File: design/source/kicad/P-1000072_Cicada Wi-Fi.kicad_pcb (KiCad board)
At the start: 2 copper layers, 40 x 65 mm, 67 parts, among them J3 Host, U1 HX3406, U3 ESP-07S

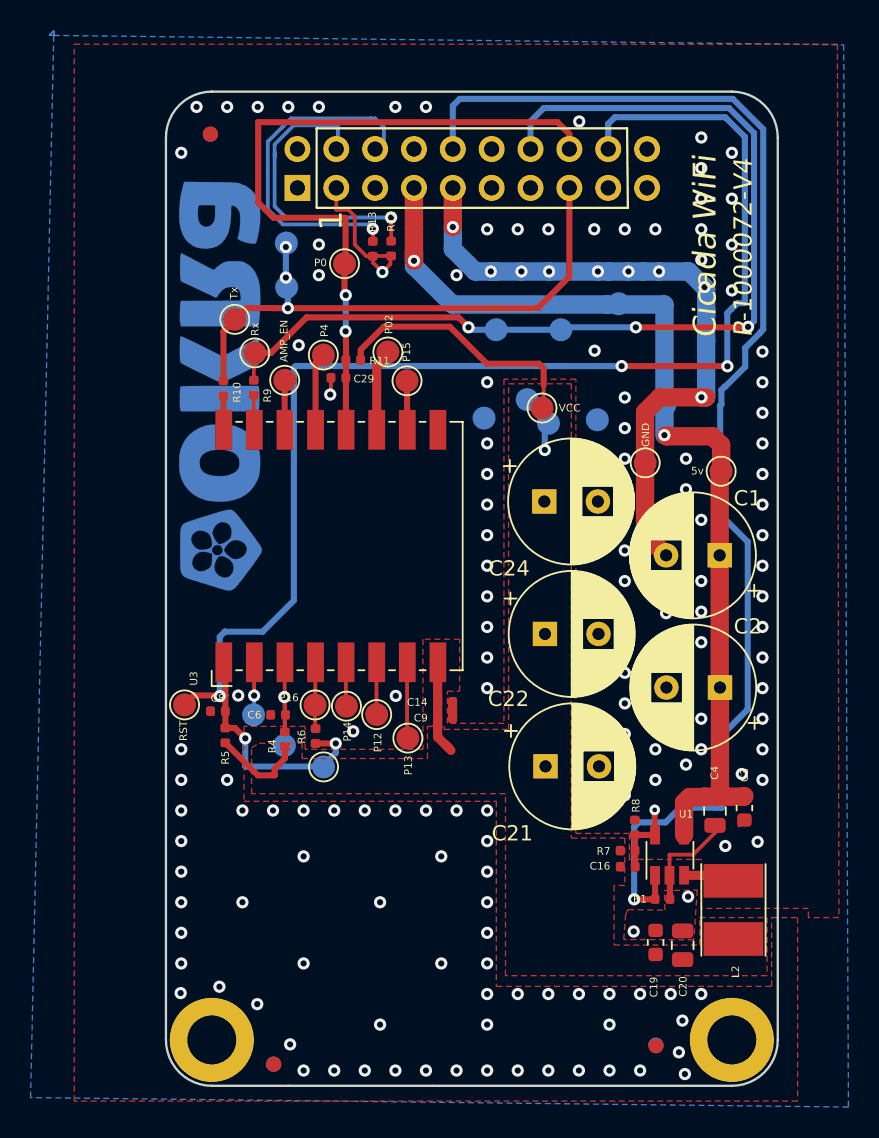
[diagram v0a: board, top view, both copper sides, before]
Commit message: P-1000072-V5.1.0_Cicada Wi-Fi Design and Manufacturing files update
Design update
1.)Inductor L2 Foot-print dimensions changed to parts commanded Foot-print dimensions(check for more information:design\doc\review\2022-03 Seed studios)
Manufacturing update
1.)updated manufacturing output files for the design change (L2 foot-print dimensions)
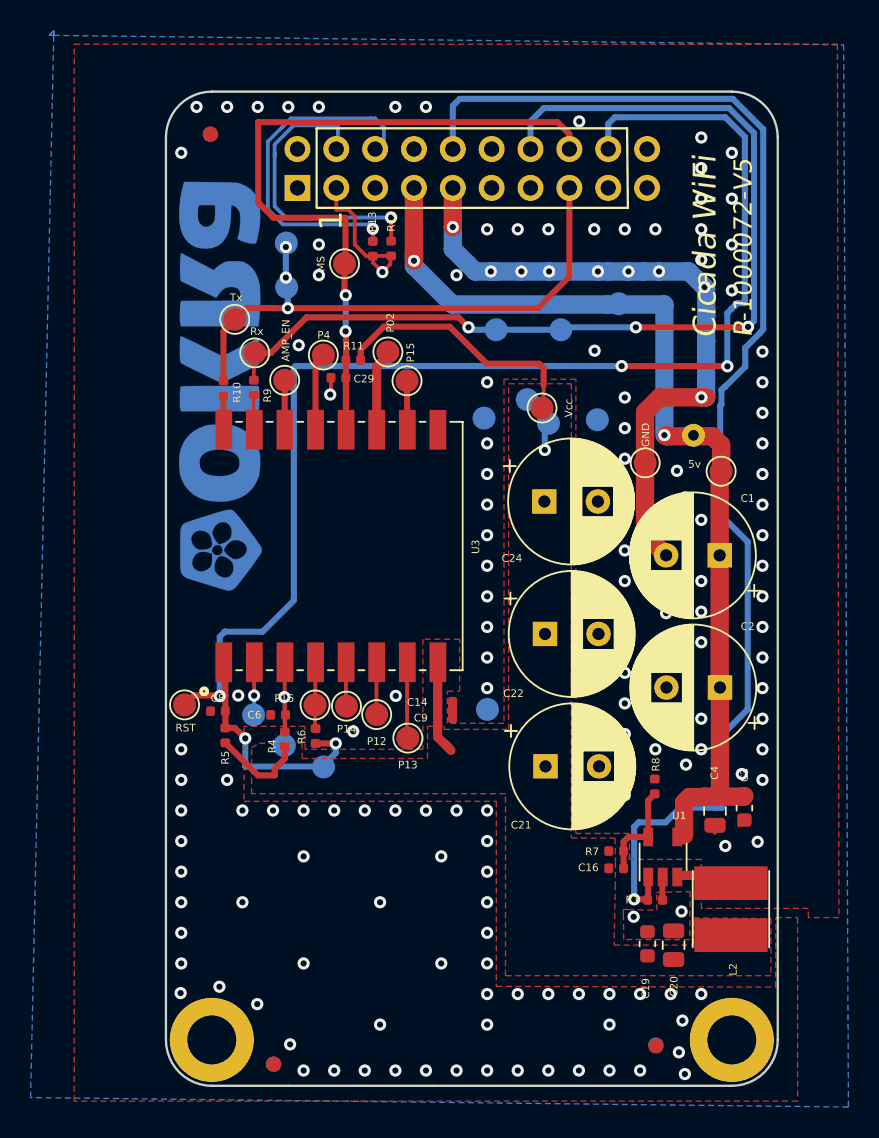
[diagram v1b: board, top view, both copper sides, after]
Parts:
- removed TP2: 5v, edemame-custom-footprints:TestPoint_Pad_D1.5mm
- added 5V: 5v, TestPoint:TestPoint_THTPad_D1.5mm_Drill0.7mm, B.Cu at (145.5, 82.5)
- added TP39: GND, okra-footprints:TestPoint_Pad_D1.5mm, B.Cu at (132.0, 100.4)
- J3: footprint cicada-footprints:PinSocket_2x08_P2.54mm_Vertical_padded -> Cicada-footprints:PinSocket_2x08_P2.54mm_Vertical_padded
- L2: footprint edemame-custom-footprints:L_4030_Handsoldering -> Cicada-footprints:L_4030_Handsoldering
- LOGO1: footprint cicada-footprints:okra_logo_copper_2 -> Cicada-footprints:okra_logo_copper_2
- TP1, TP12, TP13, TP14, TP15, TP16, TP23, TP24, TP25, TP26, TP27, TP28, TP29, TP3, TP30, TP32, TP34, TP35, TP5, TP8, TP9: footprint edemame-custom-footprints:TestPoint_Pad_D1.5mm -> okra-footprints:TestPoint_Pad_D1.5mm
- TP33: value P0 -> MS; footprint edemame-custom-footprints:TestPoint_Pad_D1.5mm -> okra-footprints:TestPoint_Pad_D1.5mm
- TP4: value VCC -> EN; footprint edemame-custom-footprints:TestPoint_Pad_D1.5mm -> okra-footprints:TestPoint_Pad_D1.5mm
- TP6: footprint edemame-custom-footprints:TestPoint_Pad_D1.5mm -> okra-footprints:TestPoint_Pad_D1.5mm; moved to B.Cu
- TP7: value VCC -> Vcc; footprint edemame-custom-footprints:TestPoint_Pad_D1.5mm -> okra-footprints:TestPoint_Pad_D1.5mm
- U3: footprint edemame-custom-footprints:ESP-07S -> Cicada-footprints:ESP-07S
- moved R8 2.99 mm to (143.0, 105.4)
- moved C16 0.76 mm to (140.4, 110.8)
- moved R7 0.75 mm to (140.4, 109.7)
- moved C20 0.59 mm to (144.2, 115.8)
- moved C19 0.54 mm to (142.5, 115.7)
- moved R1 0.49 mm to (143.0, 112.8)
- moved U1 0.46 mm to (143.5, 110.0)
- moved L2 0.17 mm to (147.9, 113.5)
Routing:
- net GND: track 56.0 -> 51.0 mm, vias 158 -> 157
- net /3V3: track 35.2 -> 33.9 mm
- net Net-(C16-Pad2): track 5.24 -> 6.47 mm, vias 1 -> 0
- net /POWER_EN: track 85.5 -> 84.5 mm
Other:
- board text added: "P-1000072-V5"
- board text removed: "P-1000072-V4"
